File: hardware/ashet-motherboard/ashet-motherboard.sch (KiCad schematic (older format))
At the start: 0 parts

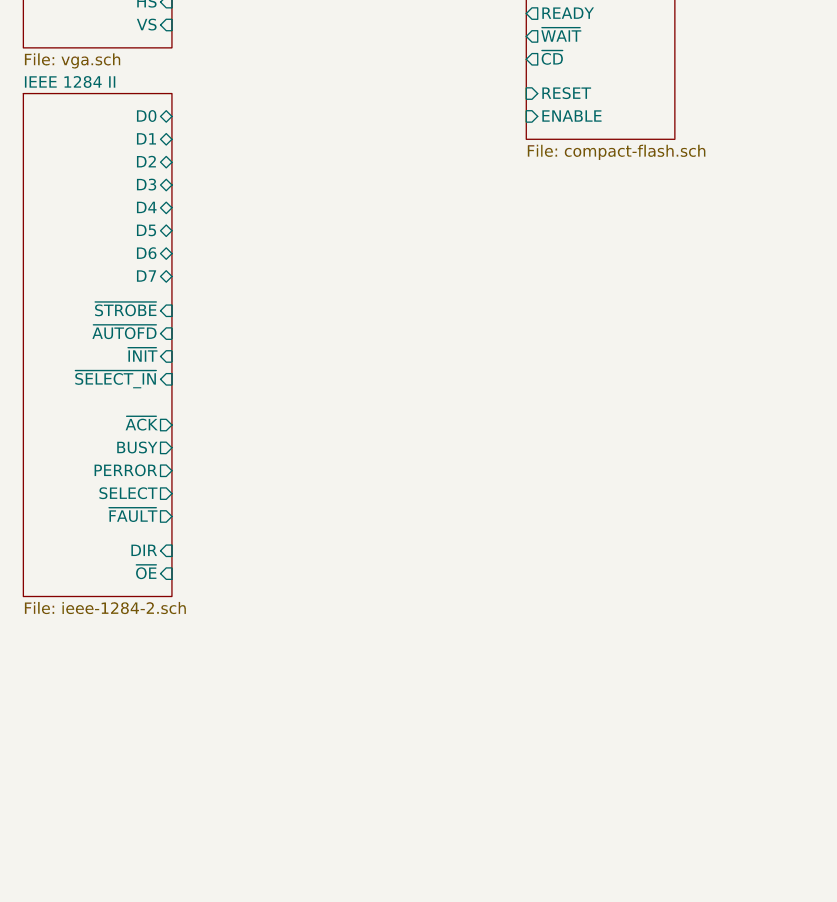
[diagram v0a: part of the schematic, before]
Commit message: schematics for pcm audio and ps/2.
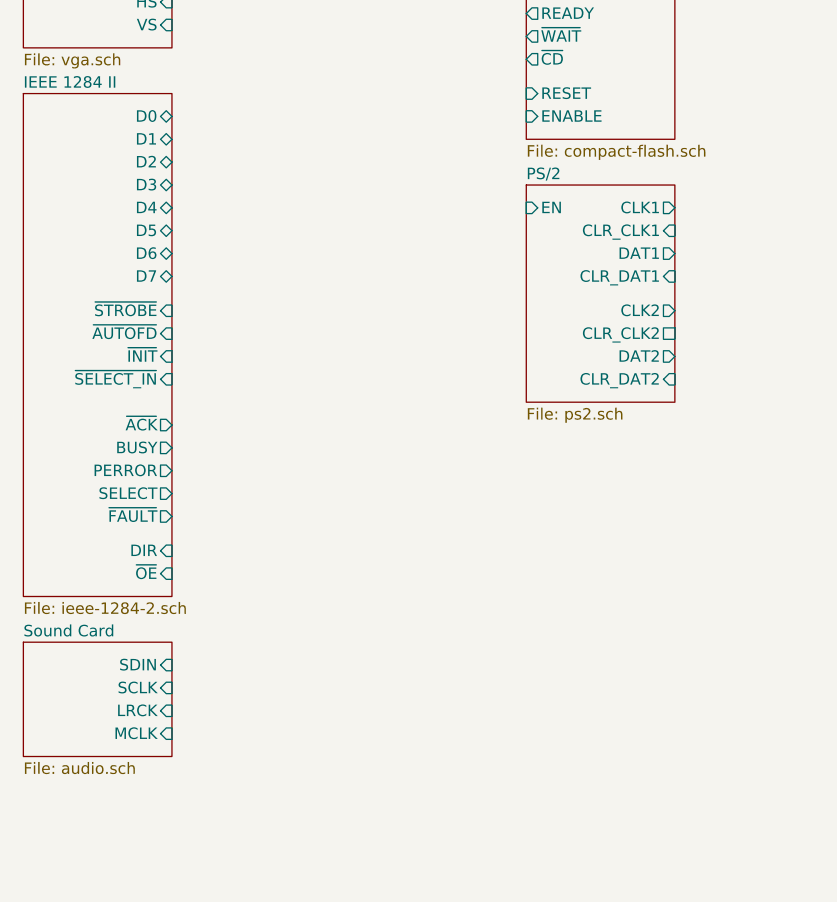
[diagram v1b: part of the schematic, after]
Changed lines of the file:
@@
 $Descr A4 11693 8268
 encoding utf-8
-Sheet 1 10
+Sheet 1 12
 Title ""
 Date ""
@@
 F38 "RESET" I L 2750 2900 50
 $EndSheet
+$Sheet
+S 2750 3300 650  950
+U 61EE171D
+F0 "PS/2" 50
+F1 "ps2.sch" 50
+F2 "CLK1" O R 3400 3400 50
+F3 "CLK2" O R 3400 3850 50
+F4 "DAT1" O R 3400 3600 50
+F5 "DAT2" O R 3400 4050 50
+F6 "CLR_CLK1" I R 3400 3500 50
+F7 "CLR_CLK2" U R 3400 3950 50
+F8 "CLR_DAT1" I R 3400 3700 50
+F9 "CLR_DAT2" I R 3400 4150 50
+F10 "EN" I L 2750 3400 50
+$EndSheet
+$Sheet
+S 550  5300 650  500
+U 61F81FE1
+F0 "Sound Card" 50
+F1 "audio.sch" 50
+F2 "SDIN" I R 1200 5400 50
+F3 "LRCK" I R 1200 5600 50
+F4 "MCLK" I R 1200 5700 50
+F5 "SCLK" I R 1200 5500 50
+$EndSheet
 $EndSCHEMATC
